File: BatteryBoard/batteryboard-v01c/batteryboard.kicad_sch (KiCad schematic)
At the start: 29 parts, among them J1 KEYSTONE-1042, J2 KEYSTONE-1042, J3 KEYSTONE-1042, J4 KEYSTONE-1042, J5 KEYSTONE-1042, J6 KEYSTONE-1042, J7 5023520601, J8 Screw_Terminal_01x02, Q1 IRF7458, Q2 IRF7458, Q3 MMBT2222AT, U1 R5460N233AF

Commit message: Added Sapling Files
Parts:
- removed Q3: MMBT2222AT, Package_TO_SOT_THT:TO-39-3, symbol Transistor_BJT:2N2219
- added Q3: MMBT2222AT, Package_TO_SOT_SMD:SOT-23, symbol Transistor_BJT:MMBT5551L
- added R7: 200k, Resistor_SMD:R_0603_1608Metric, symbol Device:R_US
- J1, J2, J3, J4, J5, J6: symbol batteryboard-rescue:1042-symbols -> batteryboard-rescue:1042-symbols-batteryboard-rescue
- J7: value 5023520601 -> MOLEX 5023520601
- R5: value 200k -> 100k
- R6: footprint Resistor_SMD:R_0603_1608Metric -> Resistor_SMD:R_1206_3216Metric
- U1: symbol batteryboard-rescue:R5460N233AF-symbols -> batteryboard-rescue:R5460N233AF-symbols-batteryboard-rescue
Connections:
- net PACK+: now also R6.1
- net PACK-: now also Q3.2 (E); no longer TH1.1
- net PyCubed_AIN5: now also TH1.1; no longer TH1.2
- net DigitalPinTBD: no longer names the net of R5.1
- net DigitalPinTBD: now also Q3.1 (B), R7.2; no longer J7.6 (Pin_6)
- new net: Q3.3 (C), TH1.2
- new net PyCubed_PA20: J7.6 (Pin_6), R7.1
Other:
- note added: "(Four power connections for increased current draw)"
- note added: "Batteries (2S3P)"
- note added: "Battery Protection"
- note added: "Connections"
- note removed: "Main Connector (Six connections for increased current draw)"
- moved on the sheet: C1, C2, C3, C4, H1, H2, H3, H4, J1, J2, J3, J4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

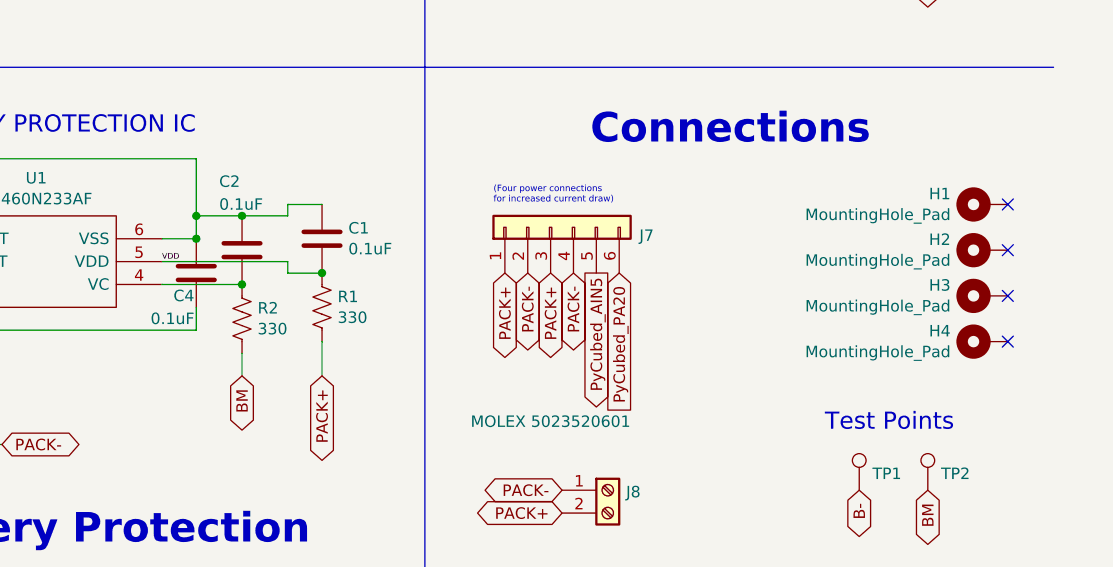
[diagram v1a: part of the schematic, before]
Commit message: Updated libraries and batteryboard/solarpanelboards accordingly
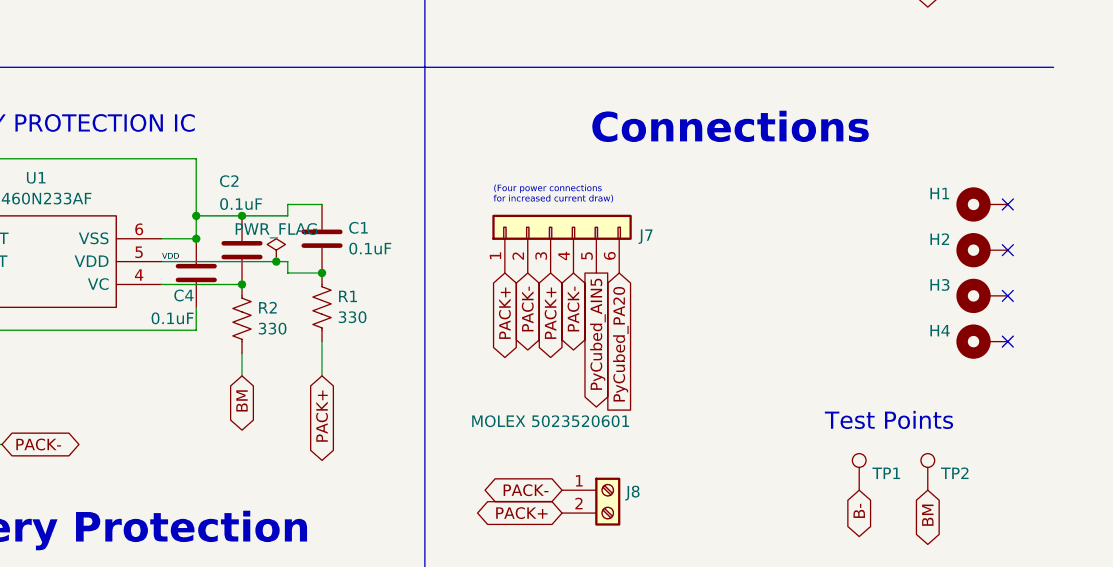
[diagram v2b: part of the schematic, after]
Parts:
- H1, H2, H3, H4: value MountingHole_Pad -> (none); footprint custom-footprints:MountingHole_3.2mm_M3_DIN965_PadMOD -> (none); now left out of the parts list
- J1, J2, J3, J4, J5, J6: symbol batteryboard-rescue:1042-symbols-batteryboard-rescue -> batteryboard:Keystone-1042
- U1: footprint custom-footprints:SOT95P280X130-6N -> Package_TO_SOT_SMD:SOT-23-6; symbol batteryboard-rescue:R5460N233AF-symbols-batteryboard-rescue -> batteryboard:R5460N233AF
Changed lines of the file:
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@@
   (junction (at 224.79 38.1) (diameter 0) (color 0 0 0 0)
+  )
+  (junction (at 180.34 93.98) (diameter 0) (color 0 0 0 0)
   )
   (junction (at 139.7 101.6) (diameter 0) (color 0 0 0 0)
@@
     (stroke (width 0) (type default) (color 0 0 0 0))
   )
+  (wire (pts (xy 180.34 93.98) (xy 181.61 93.98))
+    (stroke (width 0) (type default) (color 0 0 0 0))
+  )
   (polyline (pts (xy 127 63.5) (xy 127 25.4))
     (stroke (width 0) (type default) (color 0 0 0 0))
   )
-  (wire (pts (xy 167.64 93.98) (xy 181.61 93.98))
+  (wire (pts (xy 167.64 93.98) (xy 180.34 93.98))
     (stroke (width 0) (type default) (color 0 0 0 0))
   )
@@
     )
   )
-  (symbol (lib_id "batteryboard-rescue:1042-symbols-batteryboard-rescue") (at 148.59 29.21 0) (unit 1)
+  (symbol (lib_id "batteryboard:Keystone-1042") (at 148.59 29.21 0) (unit 1)
     (in_bom yes) (on_board yes)
     (property "Reference" "J2" (id 0) (at 161.29 22.479 0))
@@
     (pin "2")
   )
-  (symbol (lib_id "batteryboard-rescue:1042-symbols-batteryboard-rescue") (at 123.19 29.21 0) (unit 1)
+  (symbol (lib_id "batteryboard:Keystone-1042") (at 123.19 29.21 0) (unit 1)
     (in_bom yes) (on_board yes)
     (property "Reference" "J1" (id 0) (at 135.89 22.479 0))
@@
     (pin "2")
   )
-  (symbol (lib_id "batteryboard-rescue:1042-symbols-batteryboard-rescue") (at 123.19 40.64 0) (unit 1)
+  (symbol (lib_id "batteryboard:Keystone-1042") (at 123.19 40.64 0) (unit 1)
     (in_bom yes) (on_board yes)
     (property "Reference" "J3" (id 0) (at 135.89 33.909 0))
@@
     (pin "2")
   )
-  (symbol (lib_id "batteryboard-rescue:1042-symbols-batteryboard-rescue") (at 148.59 40.64 0) (unit 1)
+  (symbol (lib_id "batteryboard:Keystone-1042") (at 148.59 40.64 0) (unit 1)
     (in_bom yes) (on_board yes)
     (property "Reference" "J4" (id 0) (at 161.29 33.909 0))
@@
     (pin "2")
   )
-  (symbol (lib_id "batteryboard-rescue:1042-symbols-batteryboard-rescue") (at 123.19 52.07 0) (unit 1)
+  (symbol (lib_id "batteryboard:Keystone-1042") (at 123.19 52.07 0) (unit 1)
     (in_bom yes) (on_board yes)
     (property "Reference" "J5" (id 0) (at 135.89 45.339 0))
@@
     (pin "2")
   )
-  (symbol (lib_id "batteryboard-rescue:1042-symbols-batteryboard-rescue") (at 148.59 52.07 0) (unit 1)
+  (symbol (lib_id "batteryboard:Keystone-1042") (at 148.59 52.07 0) (unit 1)
     (in_bom yes) (on_board yes)
     (property "Reference" "J6" (id 0) (at 161.29 45.339 0))
@@
     (pin "2")
   )
-  (symbol (lib_id "batteryboard-rescue:R5460N233AF-symbols-batteryboard-rescue") (at 139.7 91.44 0) (unit 1)
+  (symbol (lib_id "batteryboard:R5460N233AF") (at 139.7 91.44 0) (unit 1)
     (in_bom yes) (on_board yes)
     (property "Reference" "U1" (id 0) (at 153.67 84.709 0))
     (property "Value" "R5460N233AF" (id 1) (at 153.67 87.0204 0))
-    (property "Footprint" "custom-footprints:SOT95P280X130-6N" (id 2) (at 163.83 88.9 0)
+    (property "Footprint" "Package_TO_SOT_SMD:SOT-23-6" (id 2) (at 163.83 88.9 0)
       (effects (font (size 1.27 1.27)) (justify left) hide)
     )
@@
   )
   (symbol (lib_id "Mechanical:MountingHole_Pad") (at 259.08 87.63 90) (mirror x) (unit 1)
-    (in_bom yes) (on_board yes)
+    (in_bom no) (on_board yes)
     (property "Reference" "H1" (id 0) (at 255.27 86.4616 90)
       (effects (font (size 1.27 1.27)) (justify left))
     )
-    (property "Value" "MountingHole_Pad" (id 1) (at 255.27 88.773 90)
-      (effects (font (size 1.27 1.27)) (justify left))
-    )
-    (property "Footprint" "custom-footprints:MountingHole_3.2mm_M3_DIN965_PadMOD" (id 2) (at 259.08 87.63 0)
+    (property "Value" "" (id 1) (at 255.27 88.773 90)
+      (effects (font (size 1.27 1.27)) (justify left))
+    )
+    (property "Footprint" "" (id 2) (at 259.08 87.63 0)
       (effects (font (size 1.27 1.27)) hide)
     )
@@
   )
   (symbol (lib_id "Mechanical:MountingHole_Pad") (at 259.08 92.71 90) (mirror x) (unit 1)
-    (in_bom yes) (on_board yes)
+    (in_bom no) (on_board yes)
     (property "Reference" "H2" (id 0) (at 255.27 91.5416 90)
       (effects (font (size 1.27 1.27)) (justify left))
     )
-    (property "Value" "MountingHole_Pad" (id 1) (at 255.27 93.853 90)
-      (effects (font (size 1.27 1.27)) (justify left))
-    )
-    (property "Footprint" "custom-footprints:MountingHole_3.2mm_M3_DIN965_PadMOD" (id 2) (at 259.08 92.71 0)
+    (property "Value" "" (id 1) (at 255.27 93.853 90)
+      (effects (font (size 1.27 1.27)) (justify left))
+    )
+    (property "Footprint" "" (id 2) (at 259.08 92.71 0)
       (effects (font (size 1.27 1.27)) hide)
     )
@@
   )
   (symbol (lib_id "Mechanical:MountingHole_Pad") (at 259.08 97.79 90) (mirror x) (unit 1)
-    (in_bom yes) (on_board yes)
+    (in_bom no) (on_board yes)
     (property "Reference" "H3" (id 0) (at 255.27 96.6216 90)
       (effects (font (size 1.27 1.27)) (justify left))
     )
-    (property "Value" "MountingHole_Pad" (id 1) (at 255.27 98.933 90)
-      (effects (font (size 1.27 1.27)) (justify left))
-    )
-    (property "Footprint" "custom-footprints:MountingHole_3.2mm_M3_DIN965_PadMOD" (id 2) (at 259.08 97.79 0)
+    (property "Value" "" (id 1) (at 255.27 98.933 90)
+      (effects (font (size 1.27 1.27)) (justify left))
+    )
+    (property "Footprint" "" (id 2) (at 259.08 97.79 0)
       (effects (font (size 1.27 1.27)) hide)
     )
@@
   )
   (symbol (lib_id "Mechanical:MountingHole_Pad") (at 259.08 102.87 90) (mirror x) (unit 1)
-    (in_bom yes) (on_board yes)
+    (in_bom no) (on_board yes)
     (property "Reference" "H4" (id 0) (at 255.27 101.7016 90)
       (effects (font (size 1.27 1.27)) (justify left))
     )
-    (property "Value" "MountingHole_Pad" (id 1) (at 255.27 104.013 90)
-      (effects (font (size 1.27 1.27)) (justify left))
-    )
-    (property "Footprint" "custom-footprints:MountingHole_3.2mm_M3_DIN965_PadMOD" (id 2) (at 259.08 102.87 0)
+    (property "Value" "" (id 1) (at 255.27 104.013 90)
+      (effects (font (size 1.27 1.27)) (justify left))
+    )
+    (property "Footprint" "" (id 2) (at 259.08 102.87 0)
       (effects (font (size 1.27 1.27)) hide)
     )
@@
     (pin "3")
   )
+  (symbol (lib_id "power:PWR_FLAG") (at 180.34 93.98 0) (unit 1)
+    (in_bom yes) (on_board yes) (fields_autoplaced)
+    (property "Reference" "#FLG0101" (id 0) (at 180.34 92.075 0)
+      (effects (font (size 1.27 1.27)) hide)
+    )
+    (property "Value" "PWR_FLAG" (id 1) (at 180.34 90.4042 0))
+    (property "Footprint" "" (id 2) (at 180.34 93.98 0)
+      (effects (font (size 1.27 1.27)) hide)
+    )
+    (property "Datasheet" "~" (id 3) (at 180.34 93.98 0)
+      (effects (font (size 1.27 1.27)) hide)
+    )
+    (pin "1")
+  )
   (sheet_instances
     (path "/" (page "1"))
   )
   (symbol_instances
+    (path "/7873ade7-bc33-4dbe-a466-c25658eb69c9"
+      (reference "#FLG0101") (unit 1) (value "PWR_FLAG") (footprint "")
+    )
     (path "/00000000-0000-0000-0000-00005e1a25da"
       (reference "C1") (unit 1) (value "0.1uF") (footprint "Capacitor_SMD:C_0603_1608Metric")
@@
     )
     (path "/00000000-0000-0000-0000-00005e185650"
-      (reference "U1") (unit 1) (value "R5460N233AF") (footprint "custom-footprints:SOT95P280X130-6N")
-    )
-  )
+      (reference "U1") (unit 1) (value "R5460N233AF") (footprint "Package_TO_SOT_SMD:SOT-23-6")
+    )
+  )

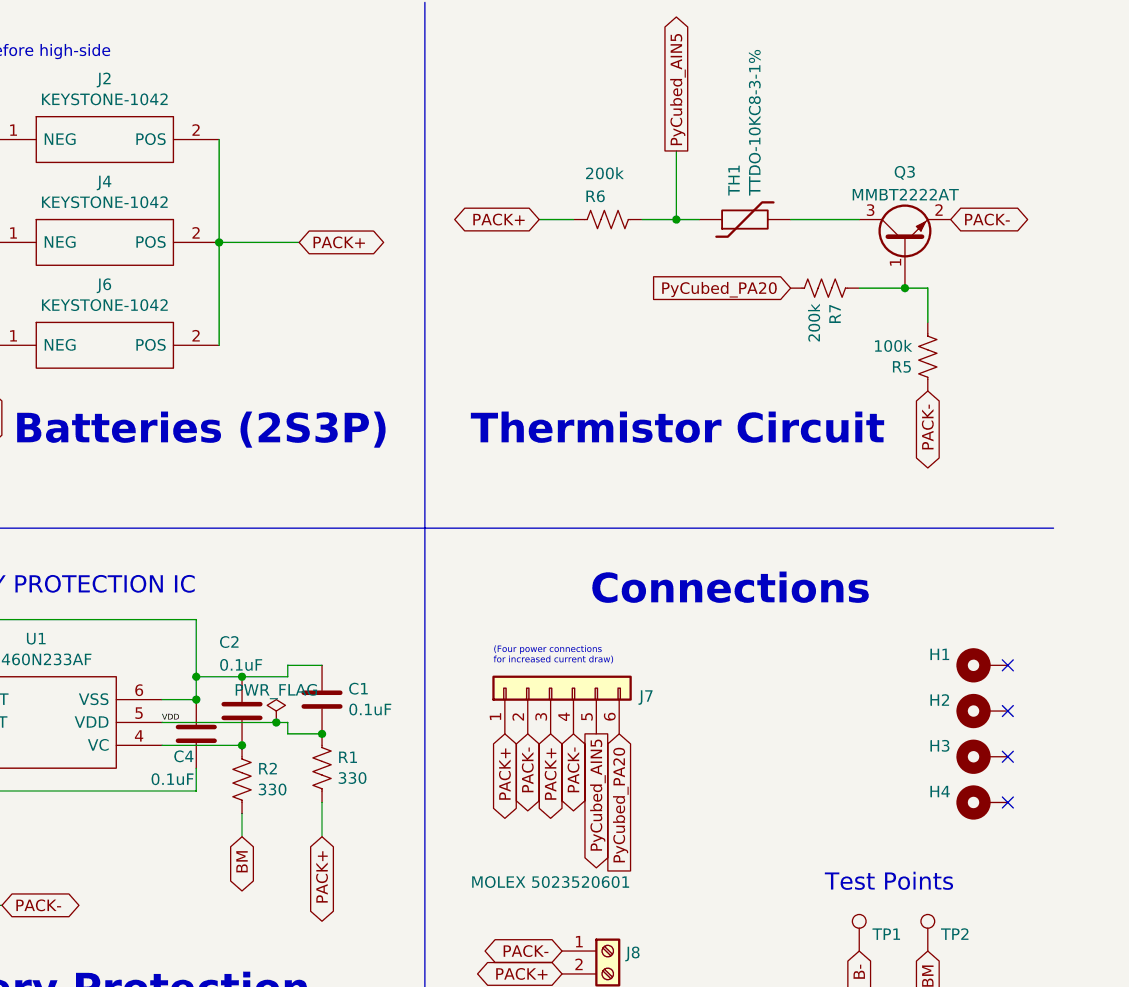
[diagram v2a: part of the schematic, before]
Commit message: Updated schematics, added/refined libraries
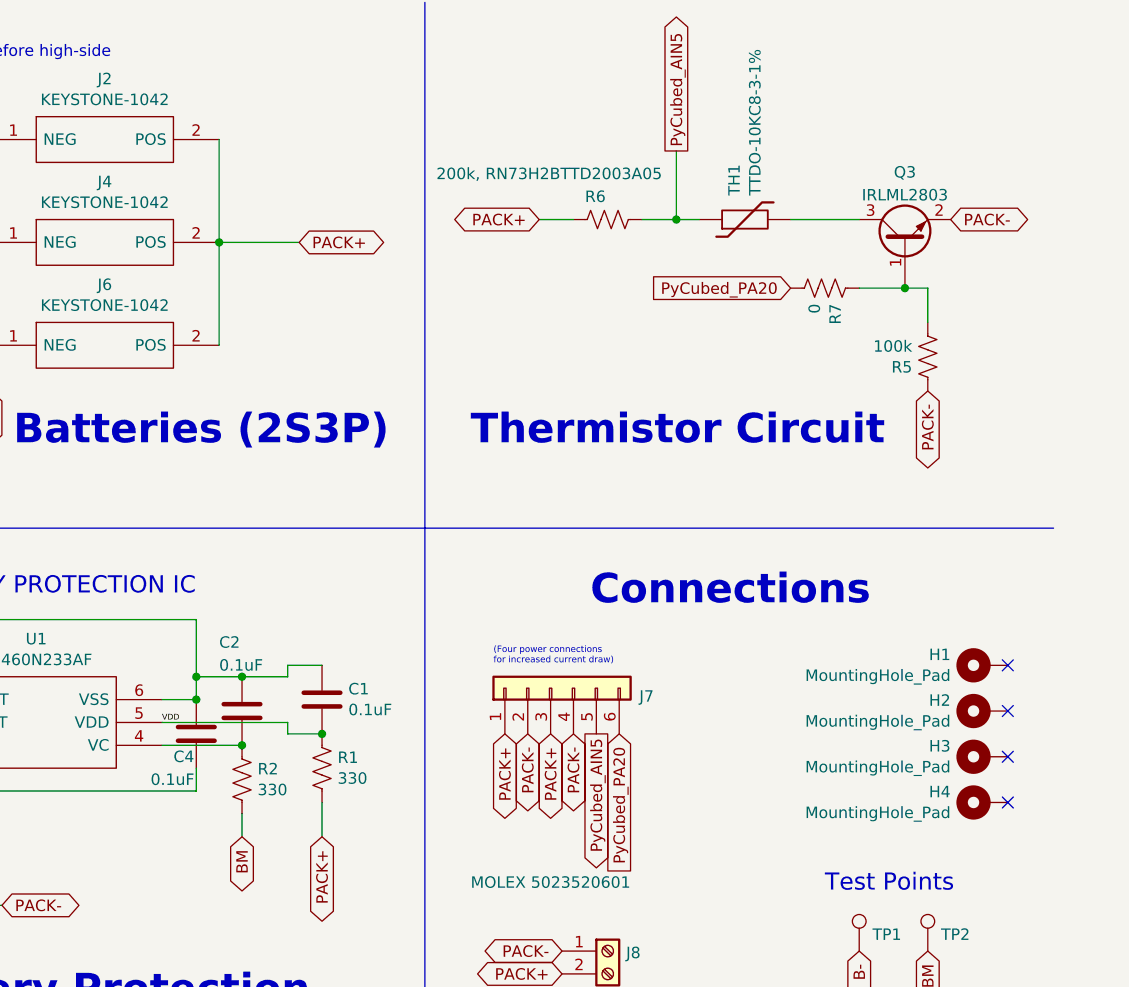
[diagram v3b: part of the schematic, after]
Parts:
- H1, H2, H3, H4: value (none) -> MountingHole_Pad; footprint (none) -> custom-footprints:MountingHole_3.2mm_M3_DIN965_PadMOD; now in the parts list
- Q3: value MMBT2222AT -> IRLML2803
- R6: value 200k -> 200k, RN73H2BTTD2003A05
- R7: value 200k -> 0

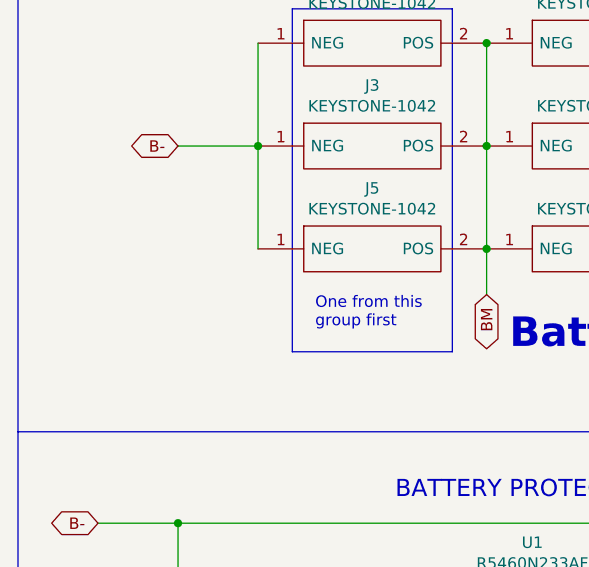
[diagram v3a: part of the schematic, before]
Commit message: incorporated 3D models into batteryboard
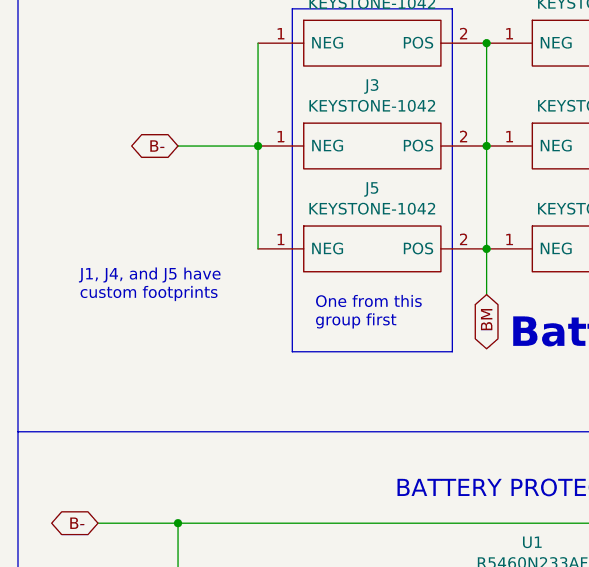
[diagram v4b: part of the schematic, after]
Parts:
- H1, H2, H3, H4: footprint custom-footprints:MountingHole_3.2mm_M3_DIN965_PadMOD -> batteryboard:MountingHole_3.2mm_M3_DIN965_PadMOD
- J1: footprint batteryboard:Keystone_1042 -> batteryboard_local:Keystone_1042_J1
- J4: footprint batteryboard:Keystone_1042 -> batteryboard_local:Keystone_1042_J4
- J5: footprint batteryboard:Keystone_1042 -> batteryboard_local:Keystone_1042_J5
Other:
- note added: "J1, J4, and J5 have custom footprints"
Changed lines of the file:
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@@
     (effects (font (size 1.905 1.905)) (justify left bottom))
+  )
+  (text "J1, J4, and J5 have\ncustom footprints" (at 103.378 57.912 0)
+    (effects (font (size 1.27 1.27)) (justify left bottom))
   )
   (text "Battery Protection" (at 137.16 125.73 0)
@@
       (effects (font (size 1.27 1.27)))
     )
-    (property "Footprint" "batteryboard:Keystone_1042" (at 144.78 26.67 0)
+    (property "Footprint" "batteryboard_local:Keystone_1042_J1" (at 144.78 26.67 0)
       (effects (font (size 1.27 1.27)) (justify left) hide)
     )
@@
       (effects (font (size 1.27 1.27)))
     )
-    (property "Footprint" "batteryboard:Keystone_1042" (at 170.18 38.1 0)
+    (property "Footprint" "batteryboard_local:Keystone_1042_J4" (at 170.18 38.1 0)
       (effects (font (size 1.27 1.27)) (justify left) hide)
     )
@@
       (effects (font (size 1.27 1.27)))
     )
-    (property "Footprint" "batteryboard:Keystone_1042" (at 144.78 49.53 0)
+    (property "Footprint" "batteryboard_local:Keystone_1042_J5" (at 144.78 49.53 0)
       (effects (font (size 1.27 1.27)) (justify left) hide)
     )
@@
       (effects (font (size 1.27 1.27)) (justify left))
     )
-    (property "Footprint" "custom-footprints:MountingHole_3.2mm_M3_DIN965_PadMOD" (at 259.08 87.63 0)
+    (property "Footprint" "batteryboard:MountingHole_3.2mm_M3_DIN965_PadMOD" (at 259.08 87.63 0)
       (effects (font (size 1.27 1.27)) hide)
     )
@@
       (effects (font (size 1.27 1.27)) (justify left))
     )
-    (property "Footprint" "custom-footprints:MountingHole_3.2mm_M3_DIN965_PadMOD" (at 259.08 92.71 0)
+    (property "Footprint" "batteryboard:MountingHole_3.2mm_M3_DIN965_PadMOD" (at 259.08 92.71 0)
       (effects (font (size 1.27 1.27)) hide)
     )
@@
       (effects (font (size 1.27 1.27)) (justify left))
     )
-    (property "Footprint" "custom-footprints:MountingHole_3.2mm_M3_DIN965_PadMOD" (at 259.08 97.79 0)
+    (property "Footprint" "batteryboard:MountingHole_3.2mm_M3_DIN965_PadMOD" (at 259.08 97.79 0)
       (effects (font (size 1.27 1.27)) hide)
     )
@@
       (effects (font (size 1.27 1.27)) (justify left))
     )
-    (property "Footprint" "custom-footprints:MountingHole_3.2mm_M3_DIN965_PadMOD" (at 259.08 102.87 0)
-      (effects (font (size 1.27 1.27)) hide)
-    )
+    (property "Footprint" "batteryboard:MountingHole_3.2mm_M3_DIN965_PadMOD" (at 259.08 102.87 0)
+      (effects (font (size 1.27 1.27)) hide)
+    )
